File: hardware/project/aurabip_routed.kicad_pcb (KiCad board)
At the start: 4 copper layers, 52 x 52 mm, 50 parts, among them J1 USB-C, J2 AKKU, J3 SPEAKER, J4 OLED SPI, J5 u.FL 868, SW1 EIN/AUS, SW2 RESET, SW3 BOOT, U1 ESP32-S3-MINI-1, U10 E22-900M22S, U2 BMP581, U3 LSM6DSO32, U4 SHT40, U5 L96, U6 MAX98357A, U7 MCP73831, U8 AP2112K-3.3, U9 USBLC6

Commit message: feat(route): deterministischer Rest-Router v4 + Gehaeuse v2 (Akustik)
- handroute4: exakte Rechteck-Kollisionspruefung (Pad-AABBs),
  Segment-Schnitttest (Kreuzungs-Bug behoben), Via-Routing F->B,
  Diagonal-/Dogleg-Kandidaten, Multi-Via-Spots, GND-Offset-Hookup;
  laeuft als LETZTER Pipeline-Schritt (kein FreeRouting-Roundtrip
  mehr danach — der SES-Import verwirft sonst Handrouten)
- LoRa-Bus (ESP<->E22 ueber Rueckseite) wird deterministisch gelegt
- Fusion-Gehaeuse v2: root.name-Fix, geschlossene Lautsprecher-
  Rueckkammer + Trichterfront + optionaler Reflex-Kanal (PORT),
  Antennen-Nische vertikal / optional SMA-Stummel (ANT_STUB),
  Akku 504050, J3 90 Grad gedreht (Ivo)

Co-Authored-By: Claude Fable 5 <noreply@anthropic.com>
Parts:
- added C16: 10u, C_0603_1608Metric, F.Cu at (26.5, 9.50)
- added R12: 0R, R_0402_1005Metric, F.Cu at (10.0, 4.80)
- added R13: 1k, R_0402_1005Metric, F.Cu at (13.5, 17.2)
- added R14: 2k, R_0402_1005Metric, F.Cu at (16.5, 17.2)
- U3: footprint Bosch_LGA-14_3x2.5mm_P0.5mm -> LGA-14_3x2.5mm_P0.5mm_LayoutBorder3x4y
- U6: footprint QFN-16-1EP_3x3mm_P0.5mm_EP1.75x1.75mm -> TQFN-16-1EP_3x3mm_P0.5mm_EP1.23x1.23mm
- moved C7 8.76 mm to (26.5, 6.30)
- moved J3 1.80 mm to (46.0, 43.5), turned to 90 degrees
- moved U5 0.90 mm to (18.0, 8.10)
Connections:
- U10 pad 10: LORA_RST -> GND
- U10 pad 11: +3V3 -> GND
- U10 pad 13: (no net) -> LORA_DIO1
- U10 pad 14: LORA_DIO1 -> LORA_BUSY
- U10 pad 15: LORA_BUSY -> LORA_RST
- U10 pad 21: (no net) -> LORA_ANT
- U10 pad 22: (no net) -> GND
- U10 pad 3: LORA_ANT -> GND
- U10 pad 4: (no net) -> GND
- U10 pad 5: (no net) -> GND
- U10 pad 6: LORA_TXEN -> LORA_RXEN
- U10 pad 7: LORA_RXEN -> LORA_TXEN
- U10 pad 9: (no net) -> +3V3
- U5 pad 1: GND -> (no net)
- U5 pad 10: GNSS_RXD -> GND
- U5 pad 11: (no net) -> GND
- U5 pad 3: GND -> (no net)
- U5 pad 4: (no net) -> GND
- U5 pad 5: (no net) -> GND
- U5 pad 6: +3V3 -> (no net)
- U5 pad 7: GND -> (no net)
- U5 pad 9: GNSS_TXD -> +3V3
- U6 pad 1: I2S_LRCK -> I2S_DOUT
- U6 pad 10: (no net) -> SPK_N
- U6 pad 11: SPK_N -> GND
- U6 pad 13: VBAT -> (no net)
- U6 pad 14: (no net) -> I2S_LRCK
- U6 pad 15: (no net) -> GND
- U6 pad 16: (no net) -> I2S_BCLK
- U6 pad 2: I2S_BCLK -> (no net)
- U6 pad 3: I2S_DOUT -> GND
- U6 pad 4: (no net) -> AMP_SD
- U6 pad 5: AMP_SD -> (no net)
- U6 pad 7: (no net) -> VBAT
- U6 pad 8: GND -> VBAT
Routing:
- net VBAT: track 18.8 -> 123.3 mm
- net I2C_SDA: track 0.00 -> 82.1 mm, vias 0 -> 4
- net I2C_SCL: track 27.5 -> 105.7 mm, vias 0 -> 2
- net TP_IO41: track 0.00 -> 53.2 mm, vias 0 -> 2
- net TP_IO40: track 0.00 -> 46.8 mm, vias 0 -> 2
- net USB_DN: track 41.7 -> 0.00 mm
- net ESP_EN: track 59.1 -> 21.6 mm, vias 0 -> 2
- net VBUS: track 2.19 -> 39.6 mm
- net OLED_RST: track 0.00 -> 24.9 mm
- net SPK_N: track 0.00 -> 24.6 mm
- net OLED_DC: track 0.00 -> 23.5 mm
- net OLED_CS: track 0.00 -> 22.6 mm
- net BTN_BOOT: track 21.3 -> 43.6 mm
- net LORA_RST: track 0.00 -> 18.6 mm, vias 0 -> 1
- net +3V3: track 13.5 -> 30.8 mm, vias 22 -> 21
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
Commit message: feat: News-Seite Juli 2026 + Gehaeuse v3 + Routing-Basis bereinigt
- docs/news: fertige Projekt-News-Seite (Renderings eingebettet,
  Explosionsansicht, Status) fuer die Website
- Gehaeuse v3: 5mm Wand, Nut/Feder-Dichtsitz, 4x M2-Inbus + Inserts,
  geschlossener Reflexkanal bis durch die Aussenwand, USB-/Schalter-
  Taschen, Display-Fenster mit exakten Waveshare-Massen (34.3x30.5,
  Glas-Versatz -0.98mm)
- Board: ungueltige Insel-Zuege entfernt, 0 DRC-Verstoesse,
  Rest-Netze als Luftlinien fuer interaktives Finish in KiCad

Co-Authored-By: Claude Fable 5 <noreply@anthropic.com>
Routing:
- net SPI2_MOSI: track 9.84 -> 76.1 mm
- net I2C_SCL: track 105.7 -> 40.4 mm
- net TP_IO41: track 53.2 -> 0.00 mm, vias 2 -> 0
- net SPI2_SCK: track 13.5 -> 65.4 mm, vias 1 -> 0
- net TP_IO40: track 46.8 -> 0.00 mm, vias 2 -> 0
- net BTN_BOOT: track 43.6 -> 4.99 mm
- net LORA_ANT: track 0.00 -> 31.0 mm
- net LORA_NSS: track 16.5 -> 0.00 mm, vias 1 -> 0
- net I2C_SDA: track 82.1 -> 65.6 mm, vias 4 -> 2
- net LORA_BUSY: track 0.00 -> 16.3 mm, vias 0 -> 1
- net CC2: track 7.70 -> 20.8 mm
- net USB_DN: track 0.00 -> 12.3 mm
- net CHG_STAT: track 5.41 -> 16.8 mm
- net I2S_LRCK: track 0.00 -> 10.8 mm
- net LORA_TXEN: track 8.58 -> 0.00 mm, vias 1 -> 0
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
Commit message: feat(route): Platine FERTIG — DRC 0 Verstoesse, 0 unverbunden
Eigener A*-Maze-Router (maze_router.py): 0.1-mm-Raster, 2 Lagen,
Via-Uebergaenge, exaktes Hindernismodell (Pads/Tracks/Vias/Moat/
Keepouts/NPTH), --narrow (5 mil), --ortho (keine Eckenschnitte),
--rip (Rip-up&Reroute), --pairs, Via-in-Pad-Rettung mit praeziser
Geometriepruefung, systematische Insel-Heilung (Waisen-Pours).

Bugs auf dem Weg: A*-f/g-Verwechslung, SWIG-__eq__, Diagonal-
Eckenschnitte, Splice-Diagonalen. I2S_DOUT per GPIO-Matrix auf
IO47 verlegt (IO6-Region war zugebaut) — Schema/Firmware-Doku folgt.

Fertigungspaket: Gerber-ZIP, Bohrdaten, Pick&Place beidseitig,
STEP-Modell. VOR BESTELLUNG: BOM-CSV neu generieren (Datei war
gesperrt) + T-H1 Teileverfuegbarkeit.

Co-Authored-By: Claude Fable 5 <noreply@anthropic.com>
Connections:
- U1 pad 10: I2S_DOUT -> (no net)
- U1 pad 27: (no net) -> I2S_DOUT
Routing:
- net I2C_SCL: track 40.4 -> 130.5 mm, vias 2 -> 5
- net TP_IO42: track 0.00 -> 70.3 mm, vias 0 -> 2
- net TP_IO41: track 0.00 -> 69.6 mm, vias 0 -> 2
- net TP_IO40: track 0.00 -> 59.1 mm, vias 0 -> 6
- net I2S_DOUT: track 0.00 -> 56.3 mm, vias 0 -> 8
- net TP_IO38: track 0.00 -> 47.0 mm, vias 0 -> 4
- net LORA_DIO1: track 0.00 -> 38.7 mm, vias 0 -> 5
- net LORA_RXEN: track 0.00 -> 33.9 mm, vias 0 -> 3
- net USB_DP: track 8.03 -> 40.3 mm, vias 0 -> 4
- net USB_DN: track 12.3 -> 40.5 mm, vias 0 -> 4
- net ESP_EN: track 29.0 -> 55.3 mm, vias 0 -> 2
- net BTN_BOOT: track 4.99 -> 27.6 mm, vias 0 -> 2
- net LORA_TXEN: track 0.00 -> 21.6 mm, vias 0 -> 3
- net I2C_SDA: track 65.6 -> 83.7 mm, vias 2 -> 4
- net GND: track 31.6 -> 46.3 mm, vias 65 -> 82
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
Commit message: fix: J3 Oeffnung zur Board-Mitte (DRC 0/0) + ADS-L-Korrektur in News/BOM/README
Keine 'Pflicht 2027'-Behauptung mehr — Standard-Kandidat ADS-L,
Hardware GFSK-faehig = ADS-L-ready per FW-Update. News-Seite mit
finalen Board-Renderings neu gebaut, Gruppenchat-Uebergabe an
@Webseite geschrieben.

Co-Authored-By: Claude Fable 5 <noreply@anthropic.com>
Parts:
- moved J3 0.50 mm to (46.5, 43.5), turned to -90 degrees
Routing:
- net SPK_N: track 23.9 -> 26.0 mm
- net SPK_P: track 24.5 -> 24.9 mm, vias 0 -> 2

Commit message: feat(emv): Review umgesetzt — Board-RF eliminiert, SPK-Paar enger
EMV-Review (Ivo) Punkt 3 nicht repariert sondern eliminiert: die
34-mm-ANT-Leitung (lag nach Modul-Flip quer ueber halbes Board, 15
Nachbarsignale) faellt weg — Flexantenne steckt DIREKT auf die
IPX-Buchse des E22-Moduls. J5 + LORA_ANT komplett entfernt
(Schema ERC 0, Board DRC 0/0). SPK_P neu als Ortho-Route neben
SPK_N (Schleifenflaeche runter). Audit bestaetigt: Innenlagen
tragen NULL Signale — GND/3V3-Planes durchgehend.

Co-Authored-By: Claude Fable 5 <noreply@anthropic.com>
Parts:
- removed J5: u.FL 868, U.FL_Hirose_U.FL-R-SMT-1_Vertical
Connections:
- U10 pad 21: LORA_ANT -> (no net)
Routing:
- net LORA_ANT: track 31.0 -> 0.00 mm
- net SPK_P: track 24.9 -> 27.4 mm

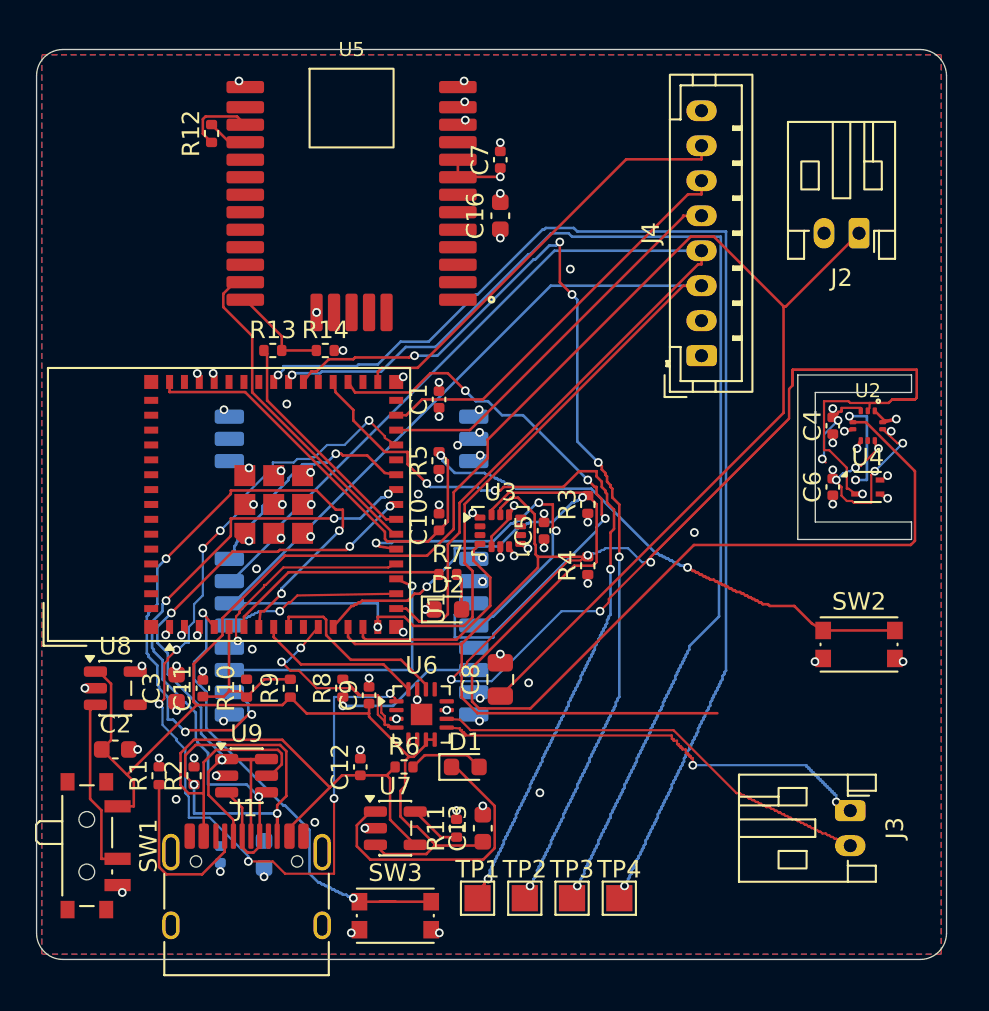
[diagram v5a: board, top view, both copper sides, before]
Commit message: wip(pcb): Via-in-Pad - 20/35 sauber per Drag-Router verschoben (DRC 0/0)
Selbstgebauter Verschiebe-Router (route/fix_via_in_pad.py): zieht Via +
angebundene Track-Enden aus dem Pad (KiCad-Drag-Prinzip), F.Cu-Stub bindet
das Pad neu an - Konnektivitaet konstruktiv erhalten. Rigoroses Kollisions-
modell inkl. interner Fraeskontur + Bohrabstand. 15 Vias in dichten Modul-
zonen noch offen (Folge-Commit).

Co-Authored-By: Claude Fable 5 <noreply@anthropic.com>
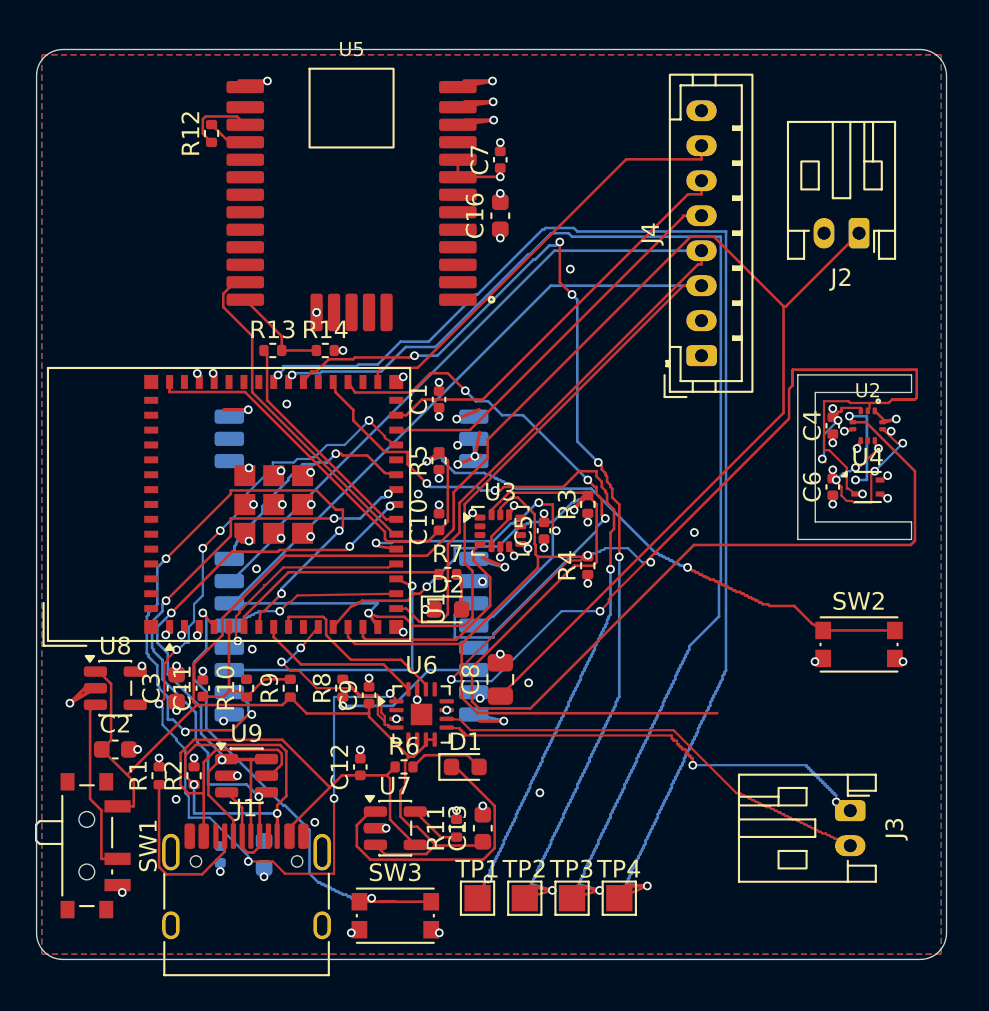
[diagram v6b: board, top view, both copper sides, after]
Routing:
- net GND: track 46.3 -> 76.0 mm
- net TP_IO42: track 70.3 -> 73.7 mm
- net TP_IO41: track 69.6 -> 72.9 mm
- net TP_IO40: track 59.1 -> 62.4 mm
- net BTN_BOOT: track 27.6 -> 30.0 mm
- net I2C_SDA: track 83.7 -> 85.9 mm
- net ESP_EN: track 55.3 -> 57.6 mm
